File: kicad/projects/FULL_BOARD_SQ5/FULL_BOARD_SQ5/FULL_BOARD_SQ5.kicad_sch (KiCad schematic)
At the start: 52 parts, among them J1 Conn_ARM_JTAG_SWD_10, J2 UART, J3 USB_C_Receptacle_USB2.0_16P, J4 CONN_2x1, Q1 BC847, SW1 TL3342F450QG, U1 24LC512, U3 AP2112K-3.3, U4 AP2112K-3.3, U73 STM32L433CCTx, Y1 NX3215SA-32.768KHZ-EXS00A-MU0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

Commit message: saving work
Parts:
- D2: footprint Package_TO_SOT_SMD_AKL:SOT-23 -> PCM_Package_TO_SOT_SMD_AKL:SOT-23
- D7: footprint Package_SO_AKL:TSOP-6_1.65x3.05mm_P0.95mm -> PCM_Package_SO_AKL:TSOP-6_1.65x3.05mm_P0.95mm
- J3: footprint Connector_USB:USB_C_Receptacle_GCT_USB4105-xx-A_16P_TopMnt_Horizontal_Modified -> Connector_USB:USB_C_Receptacle_GCT_USB4105-xx-A_16P_TopMnt_Horizontal
- Y1: footprint Crystal_AKL:Crystal_SMD_MicroCrystal_CC7V-T1A-2Pin_3.2x1.5mm_HandSoldering -> PCM_Crystal_AKL:Crystal_SMD_MicroCrystal_CC7V-T1A-2Pin_3.2x1.5mm_HandSoldering
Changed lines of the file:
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@@
 			)
 		)
-		(property "Footprint" "Connector_USB:USB_C_Receptacle_GCT_USB4105-xx-A_16P_TopMnt_Horizontal_Modified"
+		(property "Footprint" "Connector_USB:USB_C_Receptacle_GCT_USB4105-xx-A_16P_TopMnt_Horizontal"
 			(at 328.93 184.15 0)
 			(effects
@@
 			)
 		)
-		(property "Footprint" "Crystal_AKL:Crystal_SMD_MicroCrystal_CC7V-T1A-2Pin_3.2x1.5mm_HandSoldering"
+		(property "Footprint" "PCM_Crystal_AKL:Crystal_SMD_MicroCrystal_CC7V-T1A-2Pin_3.2x1.5mm_HandSoldering"
 			(at 133.35 68.58 0)
 			(effects
@@
 			)
 		)
-		(property "Footprint" "Package_SO_AKL:TSOP-6_1.65x3.05mm_P0.95mm"
+		(property "Footprint" "PCM_Package_SO_AKL:TSOP-6_1.65x3.05mm_P0.95mm"
 			(at 370.84 198.12 0)
 			(effects
@@
 			)
 		)
-		(property "Footprint" "Package_TO_SOT_SMD_AKL:SOT-23"
+		(property "Footprint" "PCM_Package_TO_SOT_SMD_AKL:SOT-23"
 			(at 328.93 31.75 0)
 			(effects

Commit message: all sensors placed and first connections
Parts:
- added J5: I2C, Connector_PinHeader_2.54mm:PinHeader_1x04_P2.54mm_Vertical, symbol Connector_Generic:Conn_01x04
- added J6: Conn_02x03_Odd_Even, Connector_PinHeader_2.54mm:PinHeader_2x03_P2.54mm_Vertical, symbol Connector_Generic:Conn_02x03_Odd_Even
- LS1, Q1, R1, R2, U1: now not fitted
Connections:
- net +3V3: now also J5.4 (Pin_4)
- net GND: now also J5.1 (Pin_1), J6.2 (Pin_2), J6.4 (Pin_4), J6.6 (Pin_6)
- net I2C_CLK: now also J5.2 (Pin_2)
- net I2C_DATA: now also J5.3 (Pin_3)
- net USER_BUTTON1: now reaches U73.26 (PB13)
- net USER_BUTTON1: now also J6.1 (Pin_1)
- net USER_BUTTON2: now reaches U73.27 (PB14)
- net USER_BUTTON2: now also J6.3 (Pin_3)
- net USER_BUTTON3: now reaches U73.28 (PB15)
- net USER_BUTTON3: now also J6.5 (Pin_5)

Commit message: some configs
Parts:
- C2, C3, Y1: now not fitted
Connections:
- net LED_ALIVE: now also U73.38 (PA15); no longer U73.18 (PB0)
- net LED_USER1: now also U73.39 (PB3); no longer U73.17 (PA7)
- net LED_USER2: now also U73.40 (PB4); no longer U73.16 (PA6)
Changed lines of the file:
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@@
 		)
 	)
-	(global_label "LED_USER2"
+	(global_label "LED_USER1"
 		(shape input)
-		(at 180.34 67.31 0)
+		(at 149.86 85.09 180)
 		(fields_autoplaced yes)
 		(effects
@@
 				(size 1.27 1.27)
 			)
-			(justify left)
+			(justify right)
 		)
 		(property "Intersheetrefs" "${INTERSHEET_REFS}"
-			(at 193.9084 67.31 0)
+			(at 136.2916 85.09 0)
 			(effects
 				(font
 					(size 1.27 1.27)
 				)
-				(justify left)
+				(justify right)
 				(hide yes)
 			)
@@
 		)
 	)
-	(global_label "LED_ALIVE"
-		(shape input)
-		(at 149.86 77.47 180)
-		(fields_autoplaced yes)
-		(effects
-			(font
-				(size 1.27 1.27)
-			)
-			(justify right)
-		)
-		(property "Intersheetrefs" "${INTERSHEET_REFS}"
-			(at 137.501 77.47 0)
-			(effects
-				(font
-					(size 1.27 1.27)
-				)
-				(justify right)
-				(hide yes)
-			)
-		)
-	)
 	(global_label "I2C_CLK"
 		(shape input)
@@
 		)
 	)
-	(global_label "LED_USER1"
-		(shape input)
-		(at 180.34 69.85 0)
-		(fields_autoplaced yes)
-		(effects
-			(font
-				(size 1.27 1.27)
-			)
-			(justify left)
-		)
-		(property "Intersheetrefs" "${INTERSHEET_REFS}"
-			(at 193.9084 69.85 0)
-			(effects
-				(font
-					(size 1.27 1.27)
-				)
-				(justify left)
-				(hide yes)
-			)
-		)
-	)
 	(global_label "MUX3"
 		(shape input)
@@
 		)
 	)
+	(global_label "LED_USER2"
+		(shape input)
+		(at 149.86 87.63 180)
+		(fields_autoplaced yes)
+		(effects
+			(font
+				(size 1.27 1.27)
+			)
+			(justify right)
+		)
+		(property "Intersheetrefs" "${INTERSHEET_REFS}"
+			(at 136.2916 87.63 0)
+			(effects
+				(font
+					(size 1.27 1.27)
+				)
+				(justify right)
+				(hide yes)
+			)
+		)
+	)
+	(global_label "LED_ALIVE"
+		(shape input)
+		(at 180.34 90.17 0)
+		(fields_autoplaced yes)
+		(effects
+			(font
+				(size 1.27 1.27)
+			)
+			(justify left)
+		)
+		(property "Intersheetrefs" "${INTERSHEET_REFS}"
+			(at 192.699 90.17 0)
+			(effects
+				(font
+					(size 1.27 1.27)
+				)
+				(justify left)
+				(hide yes)
+			)
+		)
+	)
 	(global_label "I2C_CLK"
 		(shape input)
@@
 		(in_bom yes)
 		(on_board yes)
-		(dnp no)
+		(dnp yes)
 		(property "Reference" "C3"
 			(at 131.826 73.914 0)
@@
 		)
 		(property "LCSC p/n" "C1813"
-			(at 129.54 72.39 0)
+			(at 129.54 72.39 90)
 			(effects
 				(font
@@
 		(in_bom yes)
 		(on_board yes)
-		(dnp no)
+		(dnp yes)
 		(property "Reference" "Y1"
 			(at 133.35 68.326 0)
@@
 		(in_bom yes)
 		(on_board yes)
-		(dnp no)
+		(dnp yes)
 		(property "Reference" "C2"
 			(at 133.858 60.706 0)
@@
 		)
 		(property "LCSC p/n" "C1813"
-			(at 129.54 64.77 0)
+			(at 129.54 64.77 90)
 			(effects
 				(font

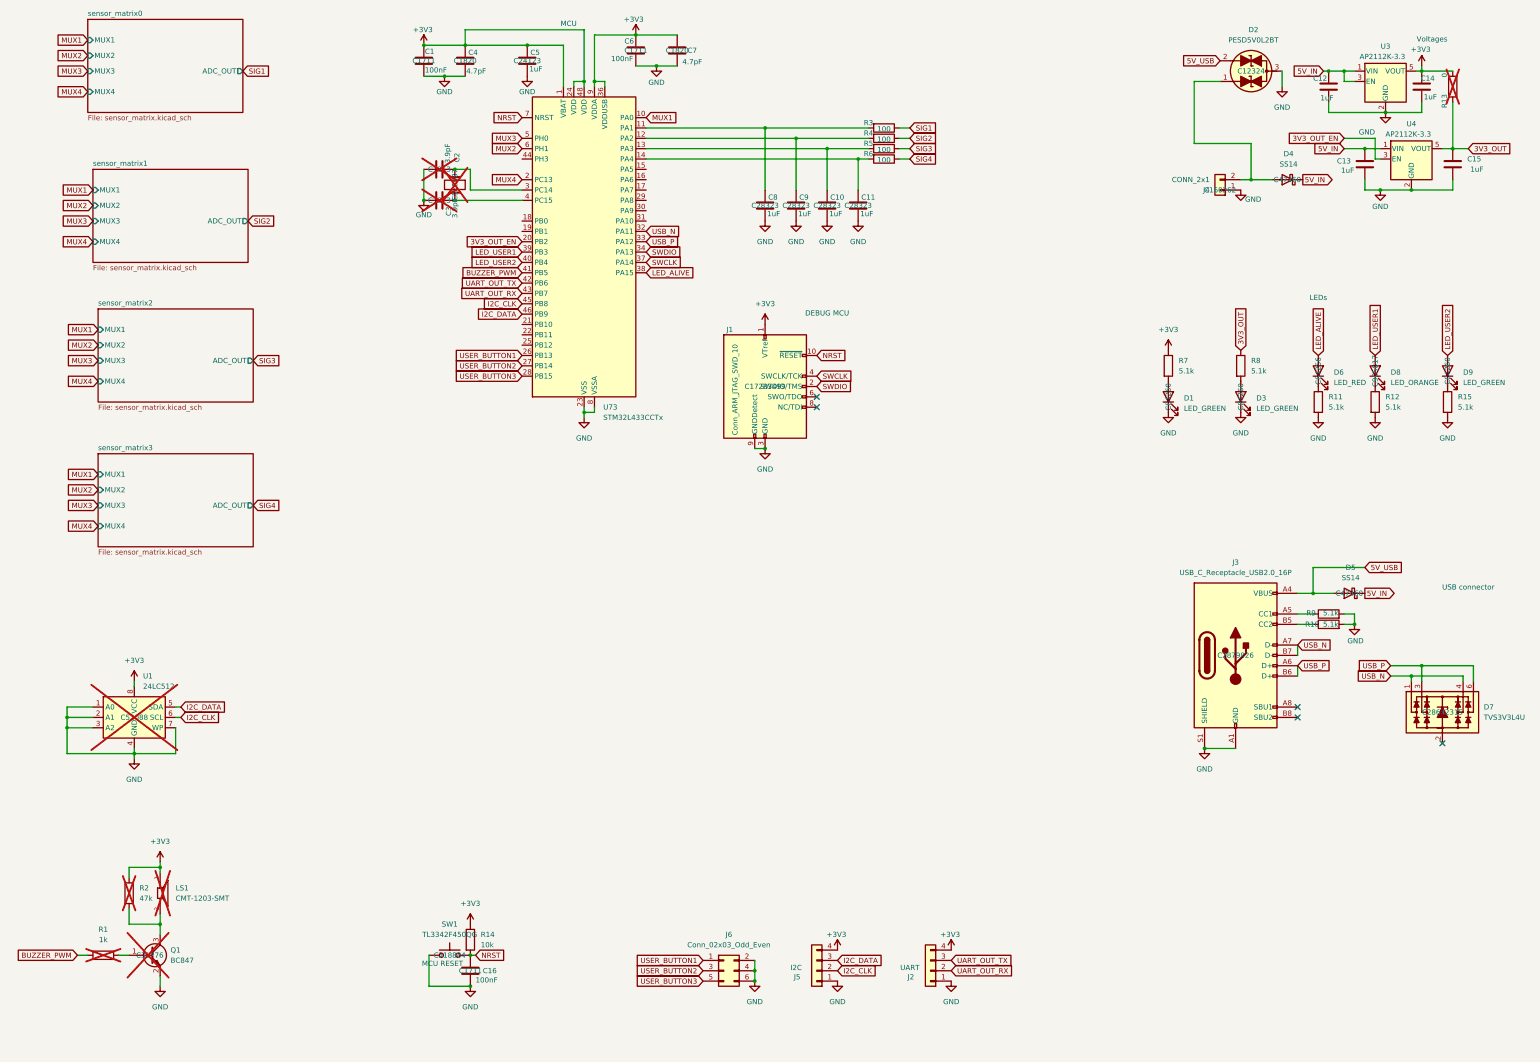
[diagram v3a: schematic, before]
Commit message: new sensors matrix board
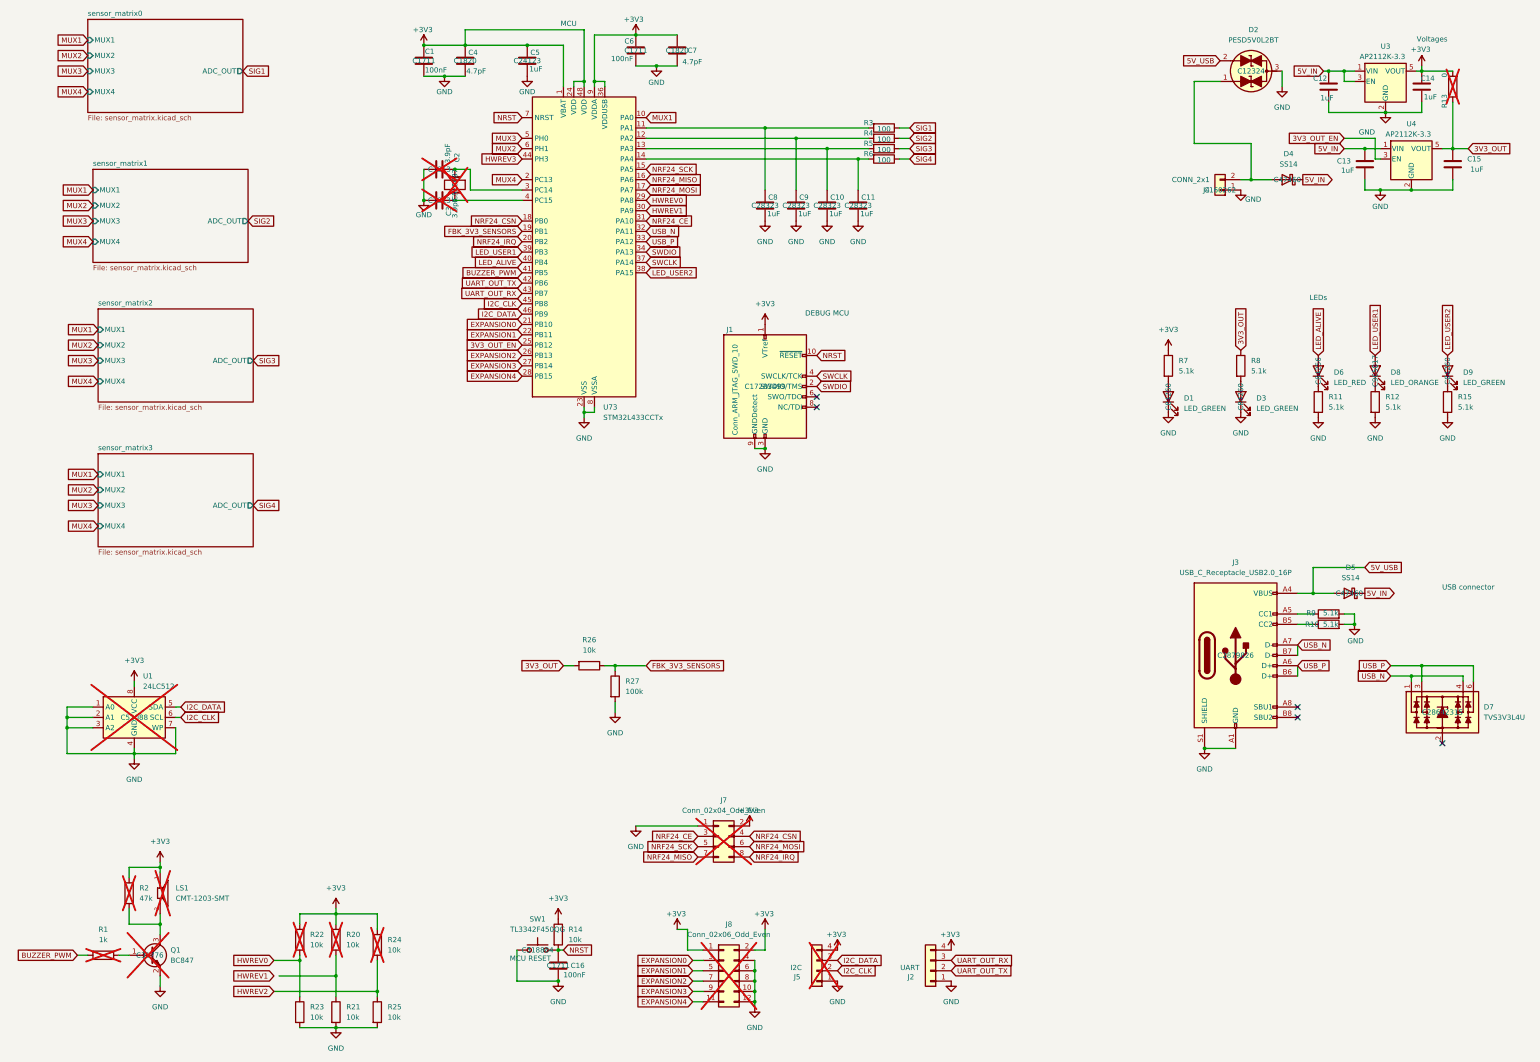
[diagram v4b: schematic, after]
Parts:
- removed J6: Conn_02x03_Odd_Even, Connector_PinHeader_2.54mm:PinHeader_2x03_P2.54mm_Vertical, symbol Connector_Generic:Conn_02x03_Odd_Even
- added J7: Conn_02x04_Odd_Even, Connector_PinSocket_2.54mm:PinSocket_2x04_P2.54mm_Vertical_SMD, symbol Connector_Generic:Conn_02x04_Odd_Even
- added J8: Conn_02x06_Odd_Even, Connector_PinHeader_2.54mm:PinHeader_2x06_P2.54mm_Vertical_SMD, symbol Connector_Generic:Conn_02x06_Odd_Even
- added R20, R21, R22, R23, R24, R25, R26: 10k, Resistor_SMD:R_0805_2012Metric_Pad1.20x1.40mm_HandSolder, symbol Device:R
- added R27: 100k, Resistor_SMD:R_0805_2012Metric_Pad1.20x1.40mm_HandSolder, symbol Device:R
- J2: footprint Connector_PinHeader_2.54mm:PinHeader_1x04_P2.54mm_Vertical -> Connector_PinHeader_2.54mm:PinHeader_1x04_P2.54mm_Horizontal
- J5: now not fitted
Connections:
- net +3V3: now also J7.2 (Pin_2), J8.1 (Pin_1), J8.2 (Pin_2), R20.1, R22.1, R24.1
- net 3V3_OUT: now also R26.2
- net 3V3_OUT_EN: now also U73.25 (PB12); no longer U73.20 (PB2)
- net GND: now also J7.1 (Pin_1), J8.10 (Pin_10), J8.12 (Pin_12), J8.4 (Pin_4), J8.6 (Pin_6), J8.8 (Pin_8), R21.2, R23.2, R25.2, R27.2
- net LED_ALIVE: now also U73.40 (PB4); no longer U73.38 (PA15)
- net LED_USER2: now also U73.38 (PA15); no longer U73.40 (PB4)
- net UART_OUT_RX: now also J2.3 (Pin_3); no longer J2.2 (Pin_2)
- net UART_OUT_TX: now also J2.2 (Pin_2); no longer J2.3 (Pin_3)
- net NRF24_SCK: now reaches U73.15 (PA5)
- net NRF24_SCK: now also J7.5 (Pin_5)
- net NRF24_MISO: now reaches U73.16 (PA6)
- net NRF24_MISO: now also J7.7 (Pin_7)
- net NRF24_MOSI: now reaches U73.17 (PA7)
- net NRF24_MOSI: now also J7.6 (Pin_6)
- net NRF24_CSN: now reaches U73.18 (PB0)
- net NRF24_CSN: now also J7.4 (Pin_4)
- net FBK_3V3_SENSORS: now reaches U73.19 (PB1)
- net FBK_3V3_SENSORS: now also R26.1, R27.1
- net EXPANSION0: now reaches U73.21 (PB10)
- net EXPANSION0: now also J8.3 (Pin_3)
- net EXPANSION1: now reaches U73.22 (PB11)
- net EXPANSION1: now also J8.5 (Pin_5)
- net HWREV0: now reaches U73.29 (PA8)
- net HWREV0: now also R22.2, R23.1
- net HWREV1: now reaches U73.30 (PA9)
- net NRF24_CE: now reaches U73.31 (PA10)
- net NRF24_CE: now also J7.3 (Pin_3)
- net HWREV3: now reaches U73.44 (PH3)
- net USER_BUTTON1 renamed EXPANSION2
- net EXPANSION2: now also J8.7 (Pin_7)
- net USER_BUTTON2 renamed EXPANSION3
- net EXPANSION3: now also J8.9 (Pin_9)
- net USER_BUTTON3 renamed EXPANSION4
- net EXPANSION4: now also J8.11 (Pin_11)
- new net: R20.2, R21.1
- new net HWREV2: R24.2, R25.1
- new net NRF24_IRQ: J7.8 (Pin_8), U73.20 (PB2)
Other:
- moved on the sheet: C16, R14, SW1
